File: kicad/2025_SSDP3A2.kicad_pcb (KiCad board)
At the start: 4 copper layers, 58.4 x 28.8 mm, 75 parts, among them J1 SolderPad, J2 SolderPad, J3 SolderPad, J4 SolderPad, J5 SolderPad, J6 SolderPad, J7 SolderPad_01x02, J8 SolderPad_1x03, Q1 CSD19537Q3, Q2 CSD19537Q3, Q3 BSZ096N10LS5, U1 LM5050-1, U2 LM5146RGYR

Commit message: Repository cleanup
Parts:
- moved C2 1.77 mm to (165.8, 118.5)
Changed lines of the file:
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@@
 	(footprint "Capacitor_SMD:C_0603_1608Metric"
 		(layer "F.Cu")
-		(at 165.5 120.25 -90)
+		(at 165.75 118.5 -90)
 		(descr "Capacitor SMD 0603 (1608 Metric), square (rectangular) end terminal, IPC_7351 nominal, (Body size source: IPC-SM-782 page 76, https://www.pcb-3d.com/wordpress/wp-content/uploads/ipc-sm-782a_amendment_1_and_2.pdf), generated with kicad-footprint-generator")
 		(tags "capacitor")
@@
 	)
 	(segment
-		(start 166.55 117.45)
-		(end 168.44 115.56)
+		(start 163.8375 119.3)
+		(end 163.8375 117.5)
 		(width 0.3)
 		(layer "F.Cu")
@@
 	)
 	(segment
-		(start 163.8375 119.3)
-		(end 165.325 119.3)
+		(start 166.55 117.45)
+		(end 168.44 115.56)
 		(width 0.3)
 		(layer "F.Cu")
@@
 	)
 	(segment
+		(start 163.8375 117.5)
+		(end 163.8875 117.45)
+		(width 0.3)
+		(layer "F.Cu")
+		(net 24)
+	)
+	(segment
 		(start 159.075 125.75)
 		(end 159.5 125.75)
@@
 		(polygon
 			(pts
-				(xy 178.45 127.175) (xy 176.575 129.05) (xy 172.95 129.05) (xy 166.75 129.05) (xy 166.75 120.75)
-				(xy 166 120) (xy 164.75 120) (xy 164.75 115.75) (xy 166.75 115.75) (xy 166.75 113) (xy 169.46736 113)
-				(xy 171.840244 114.85) (xy 178.45 114.85) (xy 178.45 119.25) (xy 178.45 125.25)
+				(xy 178.45 127.175) (xy 176.575 129.05) (xy 172.95 129.05) (xy 166.75 129.05) (xy 166.75 119) (xy 166.25 118.5)
+				(xy 164.75 118.5) (xy 164.75 115.75) (xy 166.75 115.75) (xy 166.75 113) (xy 169.46736 113) (xy 171.840244 114.85)
+				(xy 178.45 114.85) (xy 178.45 119.25) (xy 178.45 125.25)
 			)
 		)

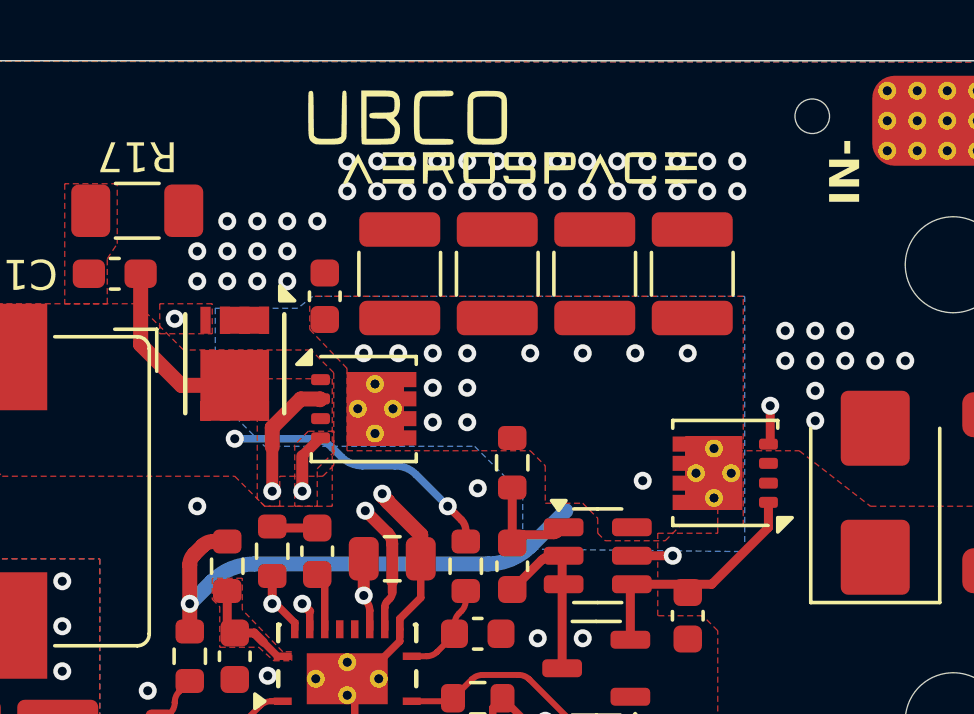
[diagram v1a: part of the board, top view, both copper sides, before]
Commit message: Removed license-restricted files
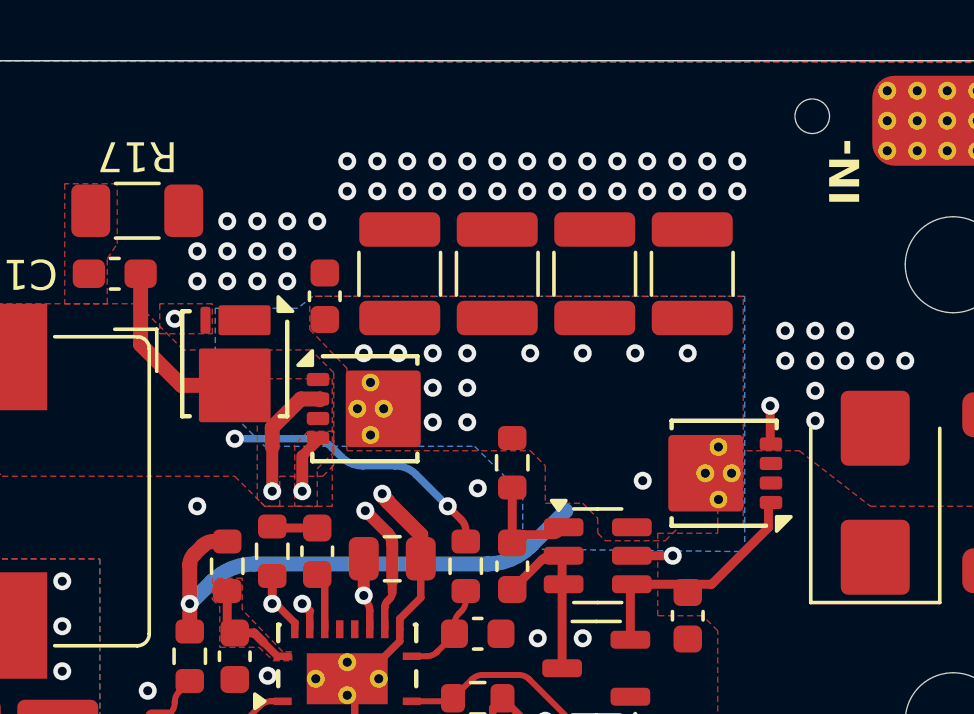
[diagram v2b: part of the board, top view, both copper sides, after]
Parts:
- removed the G*** at (159.7, 102.5)
- removed the G*** at (147.8, 110.5)
- removed the G*** at (161.8, 107.2)
- J7: footprint Connector_Custom:SolderWirePad_1x02_SMD_1.5x2mm -> Connector_Pad:SolderWirePad_1x02_SMD_1.5x2mm
- J8: footprint Connector_Custom:SolderWirePad_1x03_SMD_1.5x2mm -> Connector_Pad:SolderWirePad_1x03_SMD_1.5x2mm
- Q1, Q2: footprint Package_SON:VSON-8_3.3x3.3mm_P0.65mm_NexFET_THIN_TRACE -> Package_SON_JJ:Texas_DQG0008A_3.3x3.3mm_P0.65mm_ThermalVias-D0.3mm
- Q3: footprint TSDSON-8:PG-TSDSON-8-26 -> Package_SON_JJ:Infineon_PG-TSDSON-8-26_3.3x3.3mm_P0.65mm
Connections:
- Q3 pad 2: PGND -> /LO
- Q3 pad 3: PGND -> /SW
